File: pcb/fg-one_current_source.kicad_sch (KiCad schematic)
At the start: 11 parts, among them Q1 BC547, Q2 IRF9540N, U6 LM358

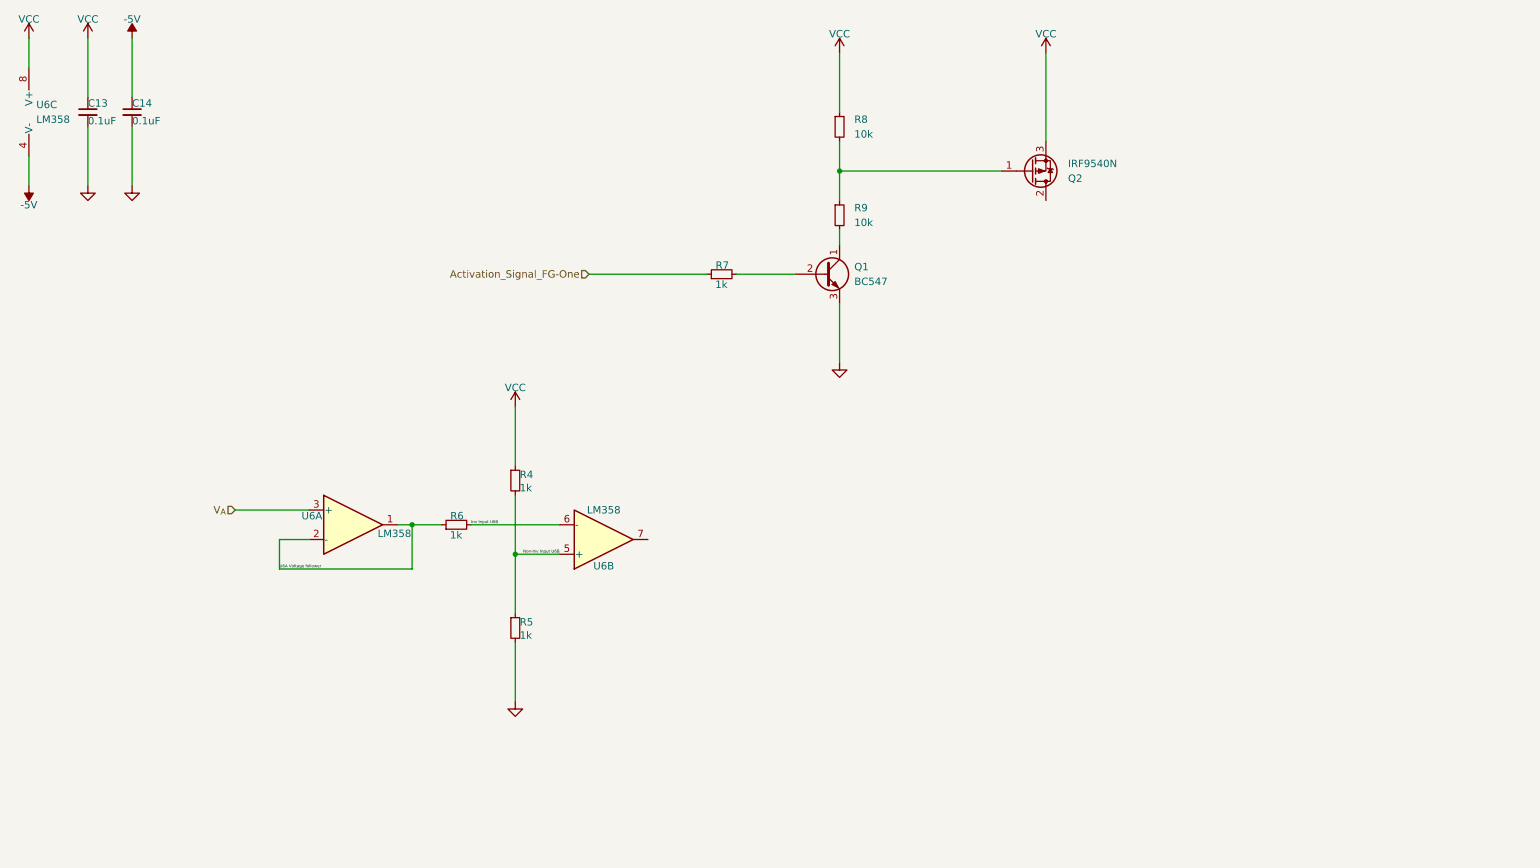
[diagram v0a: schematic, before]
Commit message: current sources added
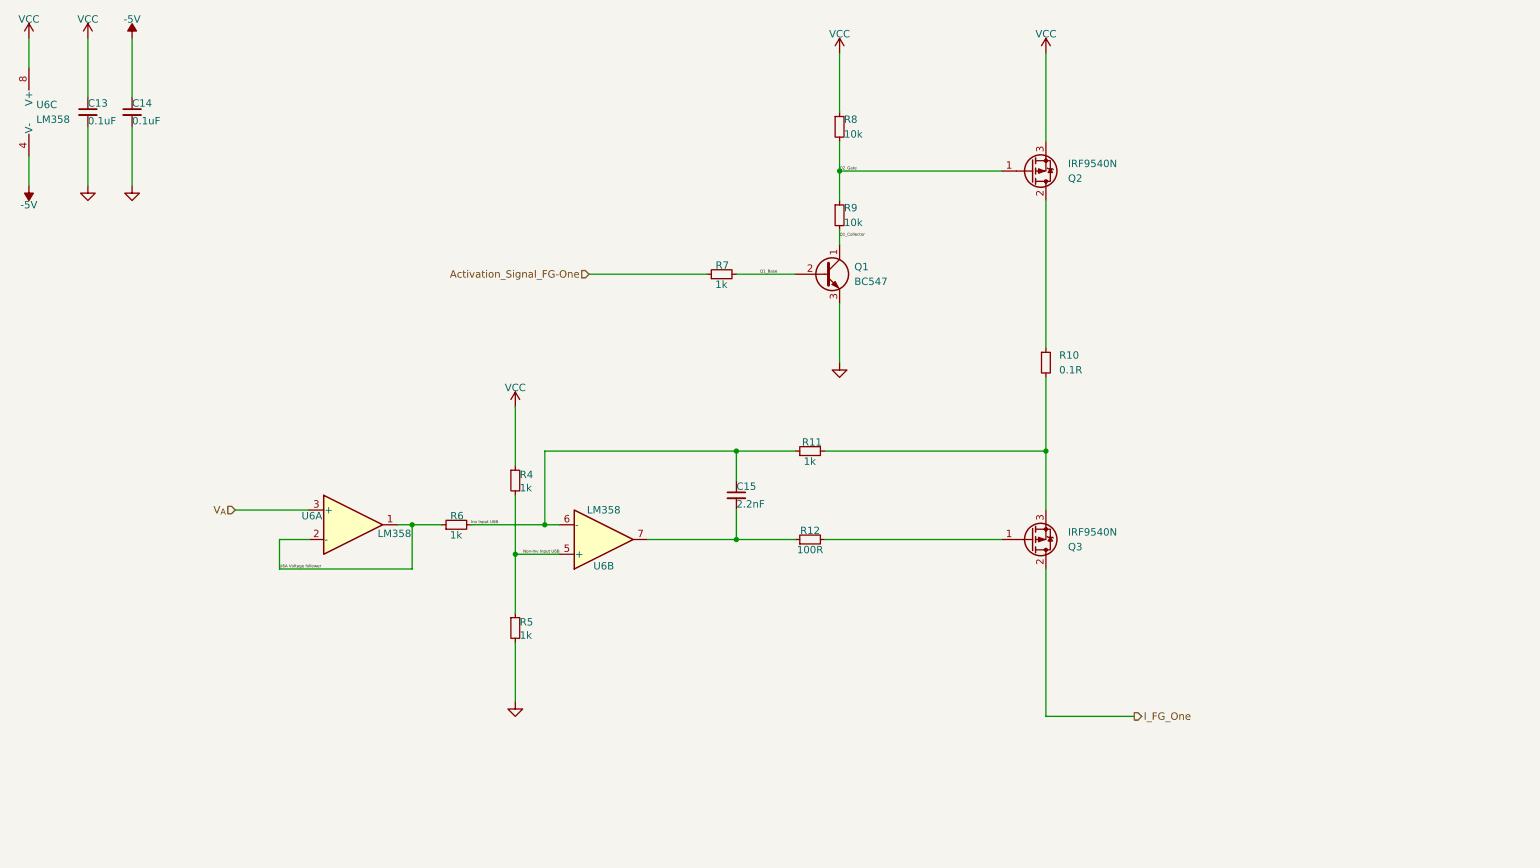
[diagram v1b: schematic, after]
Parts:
- added C15: 2.2nF, Capacitor_THT:C_Disc_D5.1mm_W3.2mm_P5.00mm, symbol Device:C_Small
- added Q3: IRF9540N, Package_TO_SOT_THT:TO-220-3_Vertical, symbol Transistor_FET:IRF9540N
- added R10: 0.1R, Resistor_THT:R_Axial_DIN0516_L15.5mm_D5.0mm_P20.32mm_Horizontal, symbol Device:R_Small
- added R11: 1k, Resistor_THT:R_Axial_DIN0207_L6.3mm_D2.5mm_P10.16mm_Horizontal, symbol Device:R_Small
- added R12: 100R, Resistor_THT:R_Axial_DIN0207_L6.3mm_D2.5mm_P10.16mm_Horizontal, symbol Device:R_Small
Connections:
- net Inv Input U6B: now also C15.1, R11.1
- net Q2_Gate: now reaches Q2.1 (G), R8.2, R9.1
- net at Q2.2 (D): now also R10.1
- net at U6.7: now also C15.2, R12.1
- net Q1_Base: now reaches Q1.2 (B), R7.2
- net Q1_Collector: now reaches Q1.1 (C), R9.2
- new net: Q3.3 (S), R10.2, R11.2
- new net: Q3.1 (G), R12.2
- new net I_FG_One: Q3.2 (D)

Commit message: current shunt measurement added
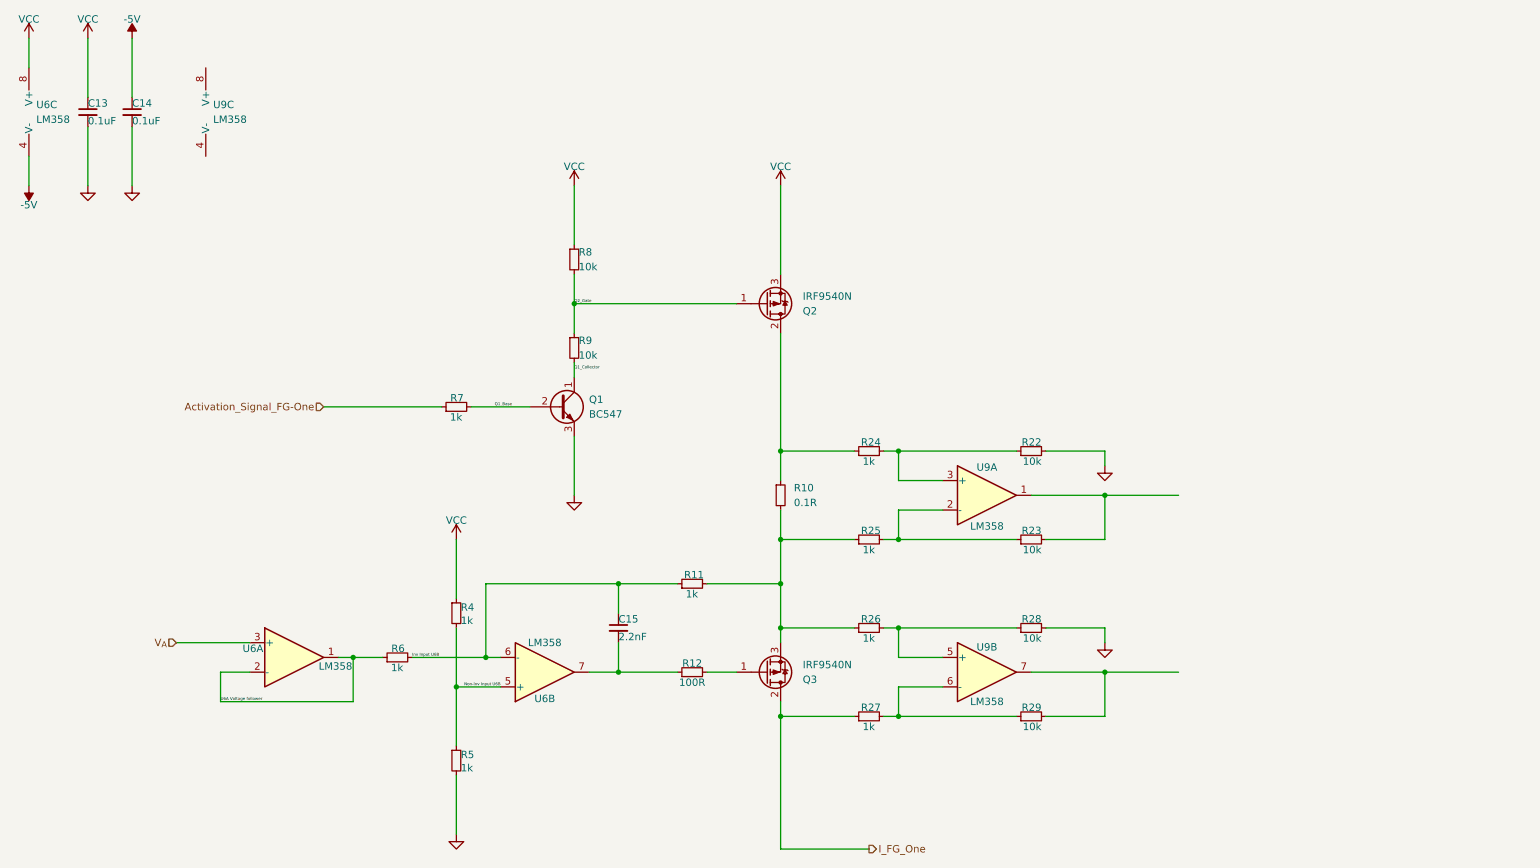
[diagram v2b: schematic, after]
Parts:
- added R22, R23, R28, R29: 10k, Resistor_THT:R_Axial_DIN0207_L6.3mm_D2.5mm_P10.16mm_Horizontal, symbol Device:R_Small
- added R24, R25, R26, R27: 1k, Resistor_THT:R_Axial_DIN0207_L6.3mm_D2.5mm_P10.16mm_Horizontal, symbol Device:R_Small
- added U9: LM358, symbol Amplifier_Operational:LM358
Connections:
- net GND: now also R22.2, R28.2
- net I_FG_One: now also R27.1
- net at Q2.2 (D), R10.1: now also R24.1
- net at Q3.3 (S), R10.2, R11.2: now also R25.1, R26.1
- new net: R23.2, U9.1
- new net: R23.1, R25.2, U9.2 (-)
- new net: R22.1, R24.2, U9.3 (+)
- new net: R26.2, R28.1, U9.5 (+)
- new net: R27.2, R29.1, U9.6 (-)
- new net: R29.2, U9.7
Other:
- moved on the sheet: C15, Q1, Q2, Q3, R10, R11, R12, R4, R5, R6, R7, R8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

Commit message: shunt measurement changed to different opamp
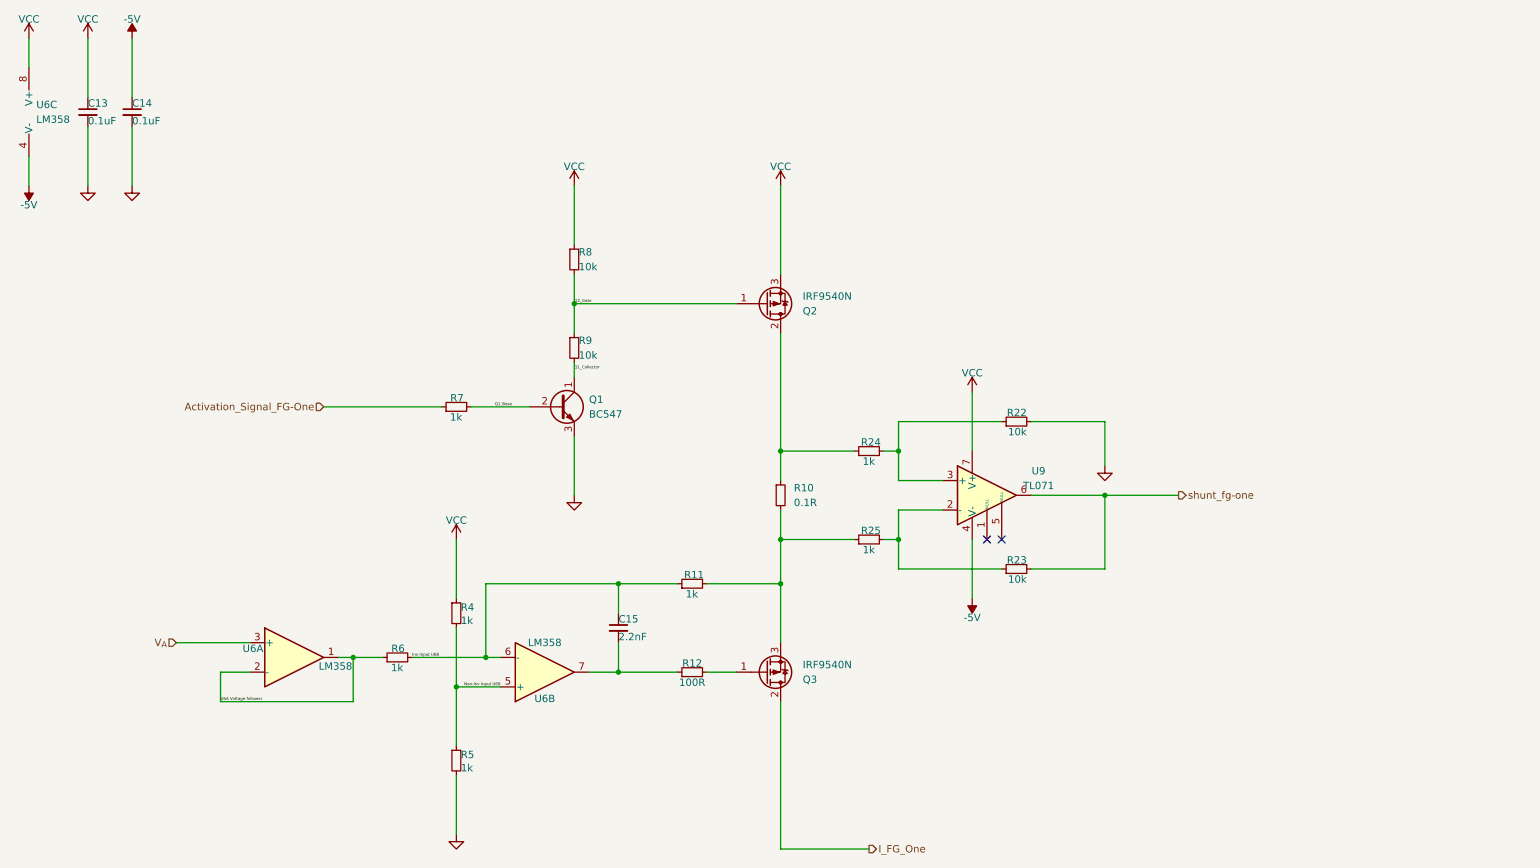
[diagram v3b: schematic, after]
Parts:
- removed R26, R27: 1k, Resistor_THT:R_Axial_DIN0207_L6.3mm_D2.5mm_P10.16mm_Horizontal, symbol Device:R_Small
- removed R28, R29: 10k, Resistor_THT:R_Axial_DIN0207_L6.3mm_D2.5mm_P10.16mm_Horizontal, symbol Device:R_Small
- removed U9: LM358, symbol Amplifier_Operational:LM358
- added U9: TL071, Package_DIP:DIP-8_W7.62mm, symbol Amplifier_Operational:TL071
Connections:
- net -5V: now also U9.4 (V-)
- net VCC: now also U9.7 (V+)
- net shunt_fg-one: now reaches R23.2
- net shunt_fg-one: now also U9.6
- net at R23.1, R25.2: now also U9.2 (-)
- net at R22.1, R24.2: now also U9.3 (+)
- no-connect marks 0 -> 2
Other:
- moved on the sheet: R22, R23

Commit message: connector added
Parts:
- Q2, Q3: footprint Package_TO_SOT_THT:TO-220-3_Vertical -> Package_TO_SOT_THT:TO-220-3_Horizontal_TabDown
- U6, U9: footprint Package_DIP:DIP-8_W7.62mm -> Package_DIP:DIP-8_W7.62mm_Socket_LongPads
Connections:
- net U6_output: now reaches C15.2, R12.1, U6.7
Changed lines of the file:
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@@
+    (effects (font (size 0.5 0.5)) (justify left bottom))
+  )
+  (label "U6_output" (at 121.92 134.62 0) (fields_autoplaced)
     (effects (font (size 0.5 0.5)) (justify left bottom))
   )
@@
       (effects (font (size 1.27 1.27)) (justify left))
     )
-    (property "Footprint" "Package_TO_SOT_THT:TO-220-3_Vertical" (at 152.4 69.215 0)
+    (property "Footprint" "Package_TO_SOT_THT:TO-220-3_Horizontal_TabDown" (at 152.4 69.215 0)
       (effects (font (size 1.27 1.27) italic) (justify left) hide)
     )
@@
       (effects (font (size 1.27 1.27)))
     )
-    (property "Footprint" "Package_DIP:DIP-8_W7.62mm" (at 186.69 102.87 0)
+    (property "Footprint" "Package_DIP:DIP-8_W7.62mm_Socket_LongPads" (at 186.69 102.87 0)
       (effects (font (size 1.27 1.27)) hide)
     )
@@
       (effects (font (size 1.27 1.27)))
     )
-    (property "Footprint" "Package_DIP:DIP-8_W7.62mm" (at 109.22 134.62 0)
+    (property "Footprint" "Package_DIP:DIP-8_W7.62mm_Socket_LongPads" (at 109.22 134.62 0)
       (effects (font (size 1.27 1.27)) hide)
     )
@@
       (effects (font (size 1.27 1.27)) (justify left))
     )
-    (property "Footprint" "Package_TO_SOT_THT:TO-220-3_Vertical" (at 152.4 132.715 0)
+    (property "Footprint" "Package_TO_SOT_THT:TO-220-3_Horizontal_TabDown" (at 152.4 132.715 0)
       (effects (font (size 1.27 1.27) italic) (justify left) hide)
     )
@@
       (effects (font (size 1.27 1.27)) (justify left))
     )
-    (property "Footprint" "Package_DIP:DIP-8_W7.62mm" (at 22.86 38.1 0)
+    (property "Footprint" "Package_DIP:DIP-8_W7.62mm_Socket_LongPads" (at 22.86 38.1 0)
       (effects (font (size 1.27 1.27)) hide)
     )
@@
       (effects (font (size 1.27 1.27)))
     )
-    (property "Footprint" "Package_DIP:DIP-8_W7.62mm" (at 66.04 132.08 0)
-      (effects (font (size 1.27 1.27)) hide)
-    )
+    (property "Footprint" "Package_DIP:DIP-8_W7.62mm_Socket_LongPads" (at 66.04 132.08 0)
+      (effects (font (size 1.27 1.27)) hide)
+    )

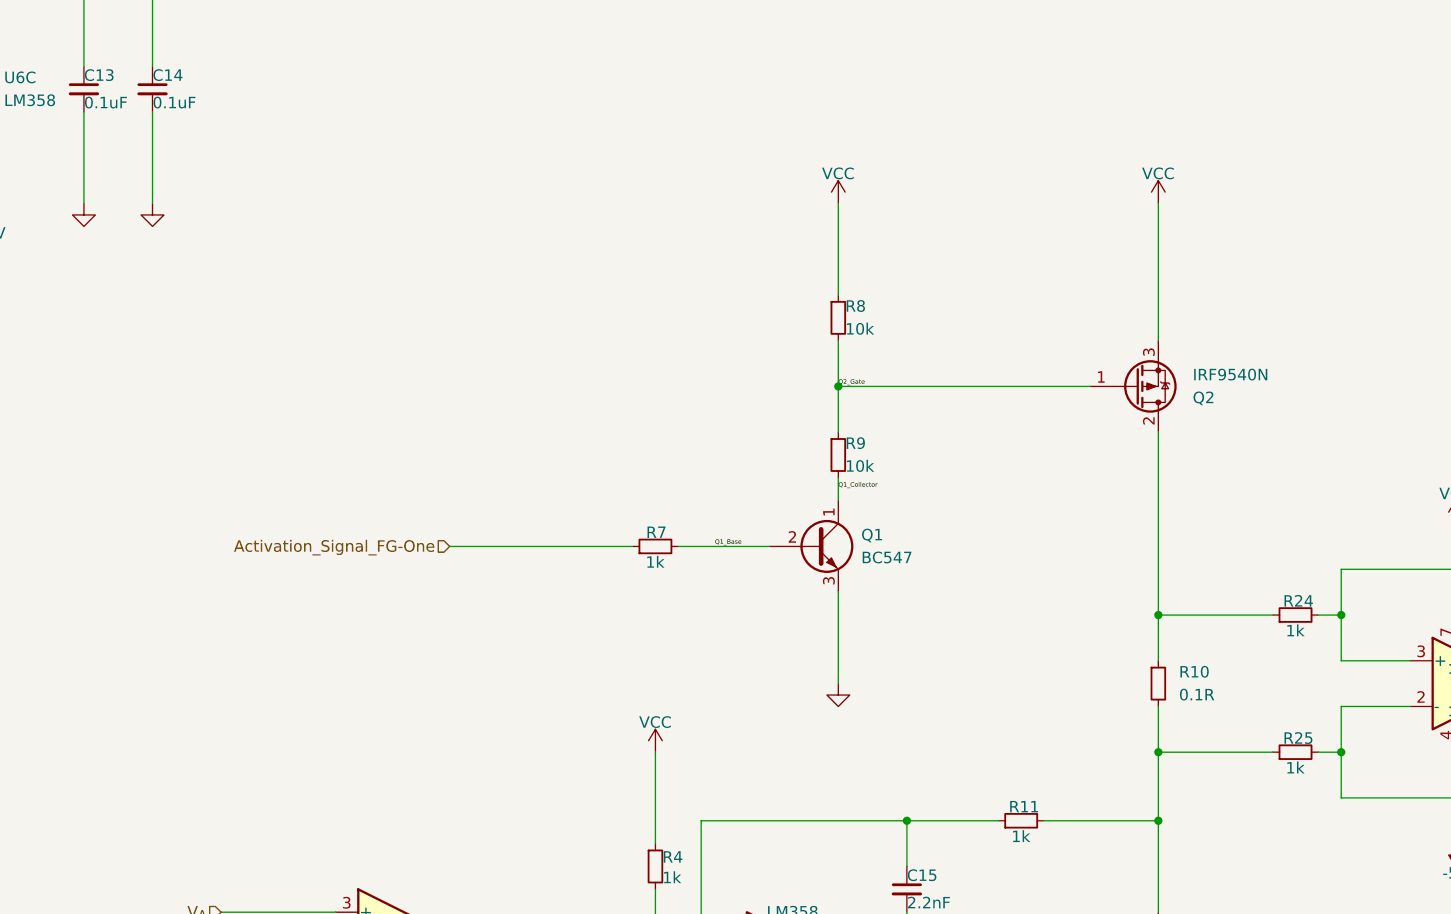
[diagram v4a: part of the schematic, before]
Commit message: potentiometer to set pwm for warm and cold light added
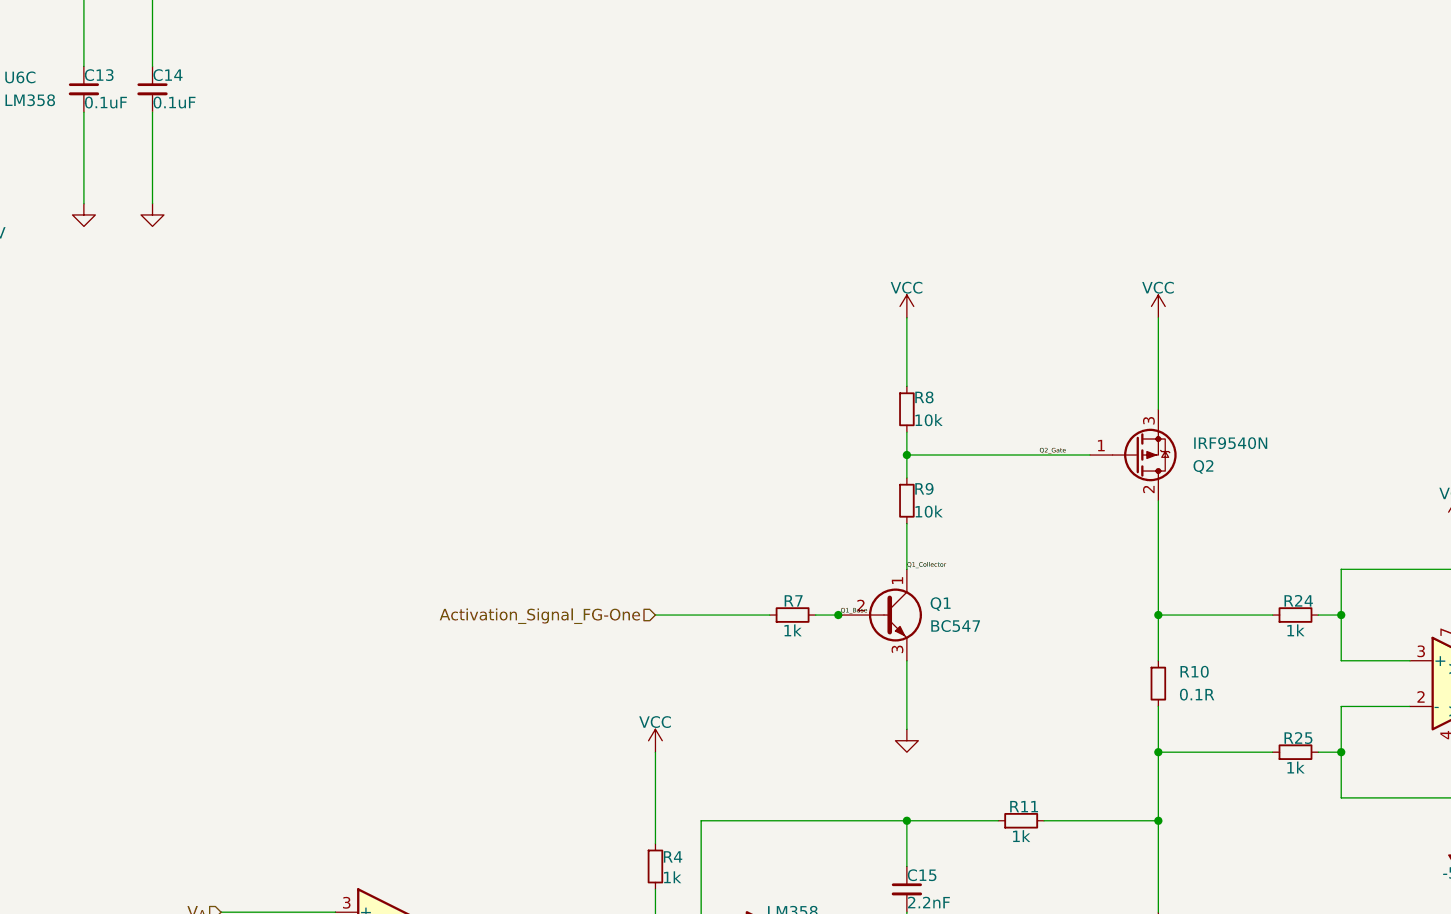
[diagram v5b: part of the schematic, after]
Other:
- moved on the sheet: Q1, Q2, R7, R8, R9

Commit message: vcc changed with +24V
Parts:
- added C13, C14: 0.1uF, Capacitor_THT:C_Disc_D5.1mm_W3.2mm_P5.00mm, symbol Device:C_Small
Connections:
- net -5V: now also C14.1
- net GND: now also C13.2, C14.2
- net VCC renamed +24V
- net +24V: now also C13.1
